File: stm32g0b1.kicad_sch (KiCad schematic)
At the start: 2 parts, among them J1 Conn_ST_STDC14, U5 STM32L432KBUx

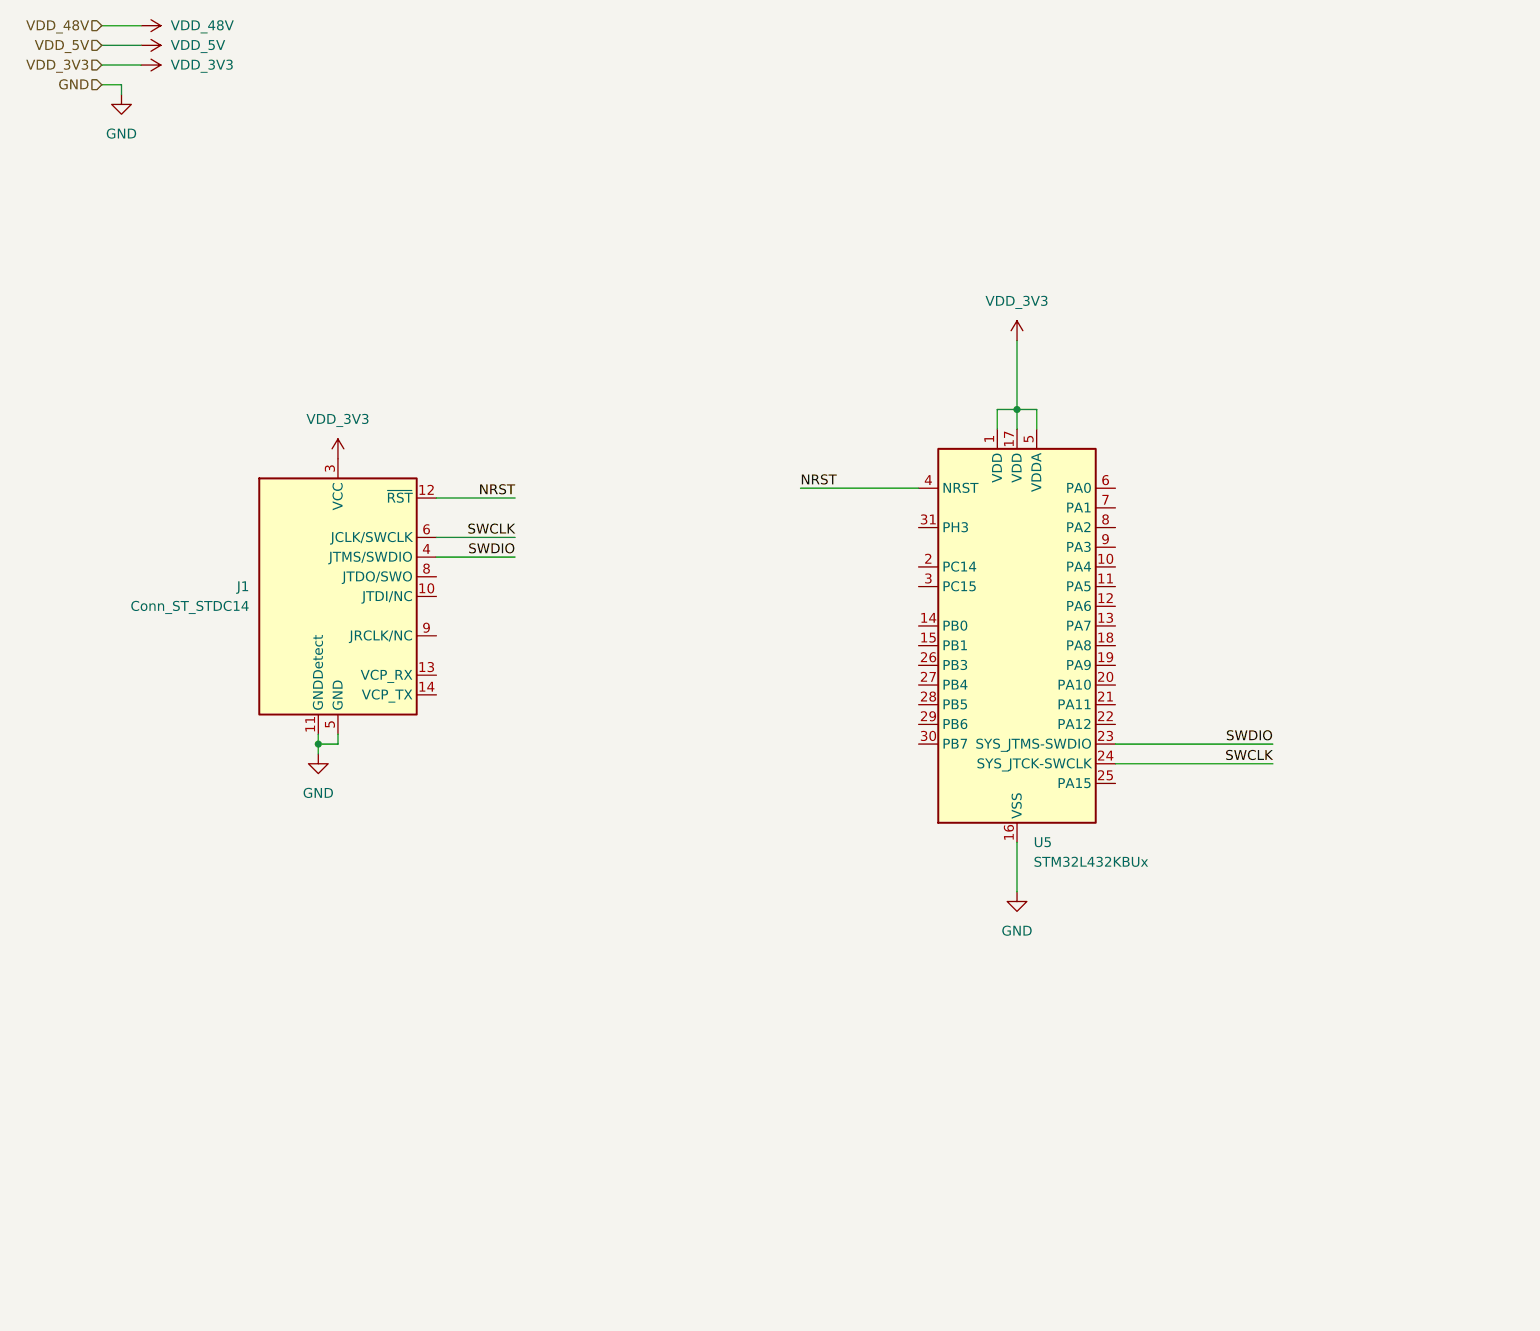
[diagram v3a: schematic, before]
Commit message: fix: fleshignout schematic for mcu, fpga and mag + peripherals
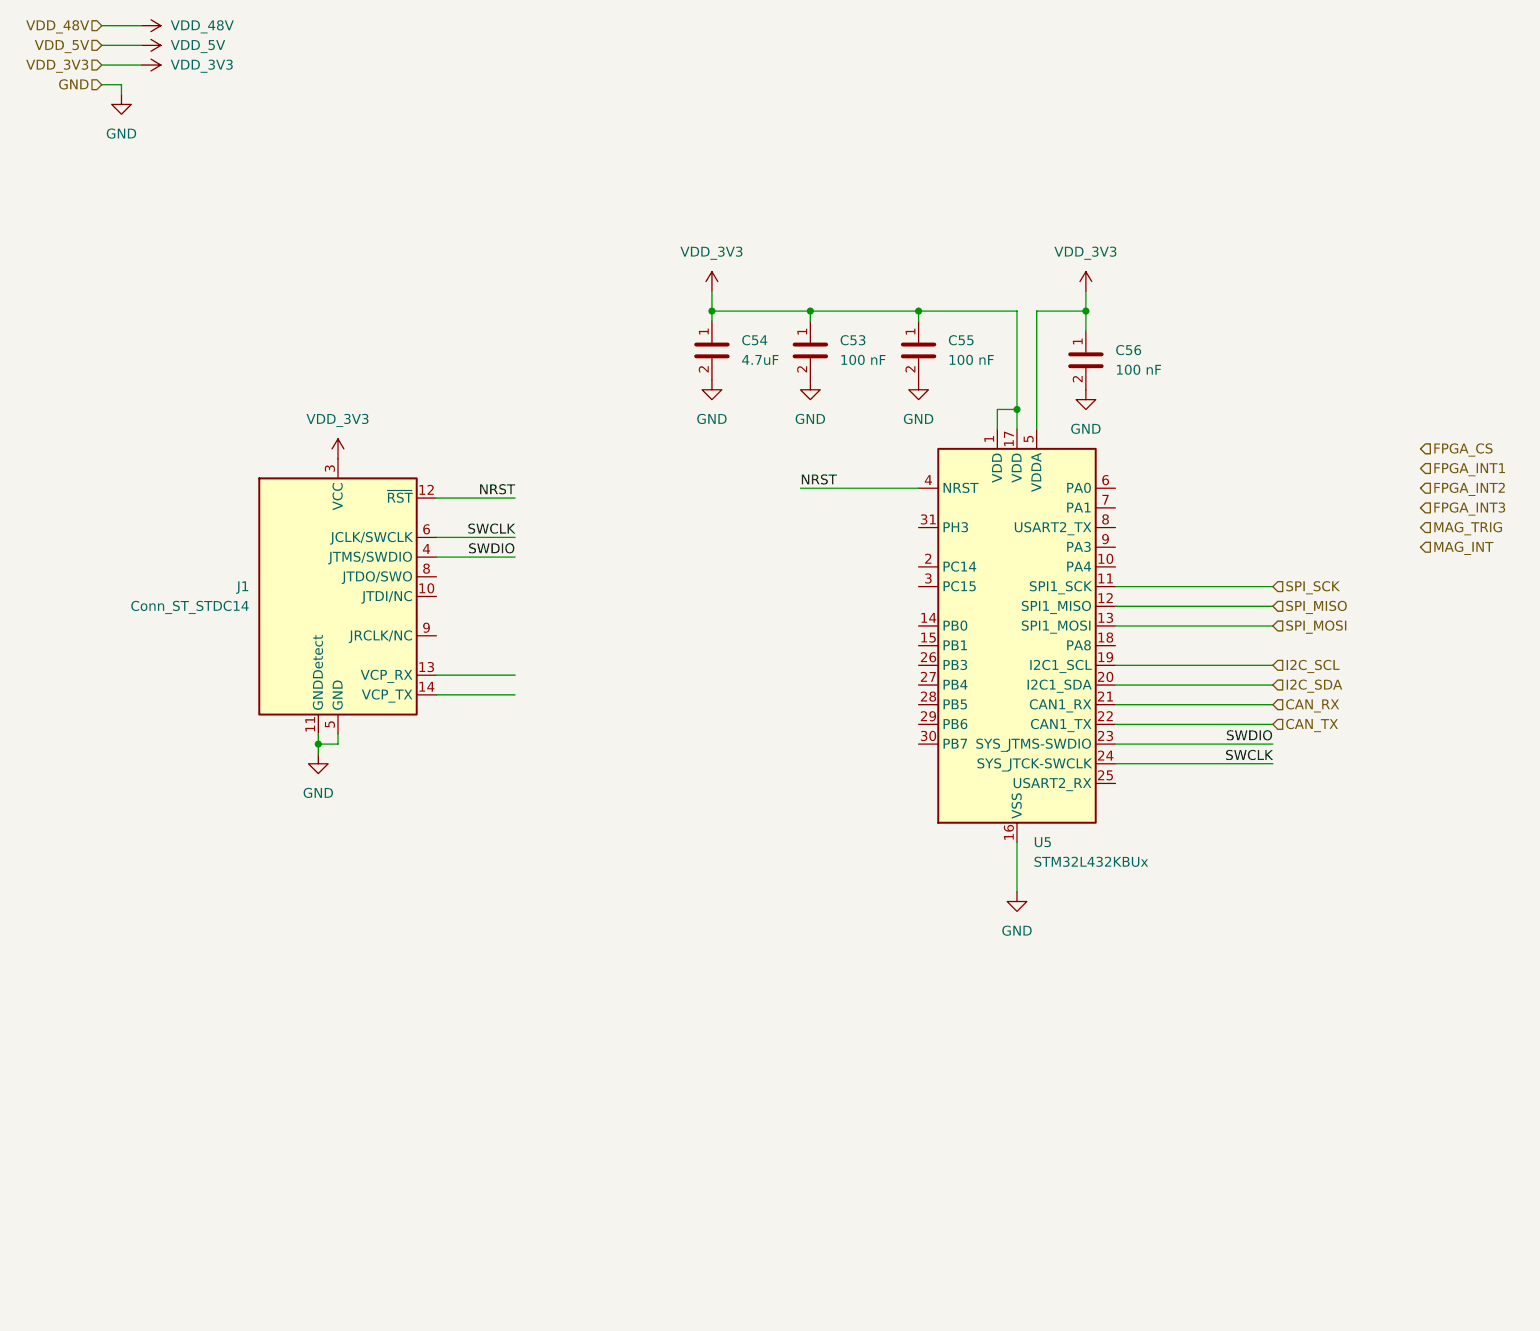
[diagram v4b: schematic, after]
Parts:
- added C53, C55, C56: 100 nF, chenry-footprint-lib:C_0402, symbol 0-chenry-component-lib:C_0402_100N
- added C54: 4.7uF, chenry-footprint-lib:C_0402, symbol 0-chenry-component-lib:C_0402_4U7
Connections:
- net GND: now also C53.2, C54.2, C55.2, C56.2
- net VDD_3V3: now also C53.1, C54.1, C55.1, C56.1
- net SPI_SCK: now reaches U5.11 (PA5)
- net SPI_MISO: now reaches U5.12 (PA6)
- net SPI_MOSI: now reaches U5.13 (PA7)
- net I2C_SCL: now reaches U5.19 (PA9)
- net I2C_SDA: now reaches U5.20 (PA10)
- net CAN_RX: now reaches U5.21 (PA11)
- net CAN_TX: now reaches U5.22 (PA12)

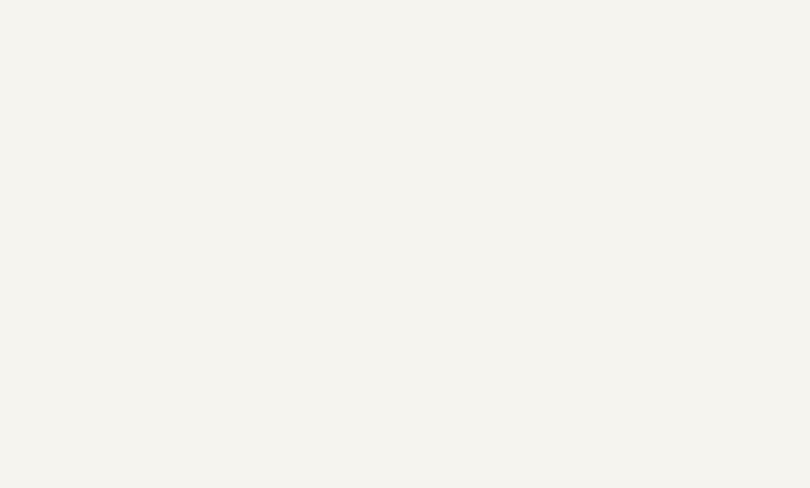
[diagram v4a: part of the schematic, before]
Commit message: fix: adjusting positioning of programmign header
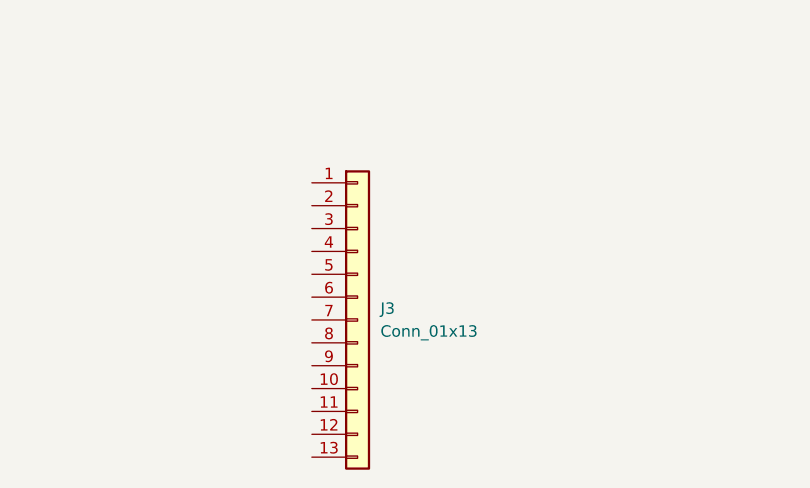
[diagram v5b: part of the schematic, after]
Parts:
- added J3: Conn_01x13, Connector_FFC-FPC:Hirose_FH12-13S-0.5SH_1x13-1MP_P0.50mm_Horizontal, symbol Connector_Generic:Conn_01x13
- J1: footprint Connector_PinHeader_1.27mm:PinHeader_2x07_P1.27mm_Vertical_SMD -> Connector_FFC-FPC:Molex_502231-1500_1x15-1SH_P0.5mm_Vertical
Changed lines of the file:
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@@
 			)
 		)
-		(property "Footprint" "Connector_PinHeader_1.27mm:PinHeader_2x07_P1.27mm_Vertical_SMD"
+		(property "Footprint" "Connector_FFC-FPC:Molex_502231-1500_1x15-1SH_P0.5mm_Vertical"
 			(at 54.61 90.17 0)
 			(effects
@@
 					(unit 1)
 				)
+			)
+		)
+	)
+	(symbol
+		(lib_id "Connector_Generic:Conn_01x13")
+		(at 57.15 166.37 0)
+		(unit 1)
+		(exclude_from_sim no)
+		(in_bom yes)
+		(on_board yes)
+		(dnp no)
+		(fields_autoplaced yes)
+		(property "Reference" "J3"
+			(at 59.69 165.0999 0)
+			(effects
+				(font
+					(size 1.27 1.27)
+				)
+				(justify left)
+			)
+		)
+		(property "Value" "Conn_01x13"
+			(at 59.69 167.6399 0)
+			(effects
+				(font
+					(size 1.27 1.27)
+				)
+				(justify left)
+			)
+		)
+		(property "Footprint" "Connector_FFC-FPC:Hirose_FH12-13S-0.5SH_1x13-1MP_P0.50mm_Horizontal"
+			(at 57.15 166.37 0)
+			(effects
+				(font
+					(size 1.27 1.27)
+				)
+				(hide yes)
+			)
+		)
+		(property "Datasheet" "~"
+			(at 57.15 166.37 0)
+			(effects
+				(font
+					(size 1.27 1.27)
+				)
+				(hide yes)
+			)
+		)
+		(property "Description" "Generic connector, single row, 01x13, script generated (kicad-library-utils/schlib/autogen/connector/)"
+			(at 57.15 166.37 0)
+			(effects
+				(font
+					(size 1.27 1.27)
+				)
+				(hide yes)
+			)
+		)
+		(property "MFR_PN1" ""
+			(at 57.15 166.37 0)
+			(effects
+				(font
+					(size 1.27 1.27)
+				)
+				(hide yes)
+			)
+		)
+		(property "MFR_PN2" ""
+			(at 57.15 166.37 0)
+			(effects
+				(font
+					(size 1.27 1.27)
+				)
+				(hide yes)
+			)
+		)
+		(property "MFR_PN3" ""
+			(at 57.15 166.37 0)
+			(effects
+				(font
+					(size 1.27 1.27)
+				)
+				(hide yes)
+			)
+		)
+		(property "JLC_PN" ""
+			(at 57.15 166.37 0)
+			(effects
+				(font
+					(size 1.27 1.27)
+				)
+				(hide yes)
+			)
+		)
+		(pin "7"
+		)
+		(pin "5"
+		)
+		(pin "10"
+		)
+		(pin "6"
+		)
+		(pin "11"
+		)
+		(pin "8"
+		)
+		(pin "9"
+		)
+		(pin "12"
+		)
+		(pin "13"
+		)
+		(pin "3"
+		)
+		(pin "1"
+		)
+		(pin "2"
+		)
+		(pin "4"
+		)
+		(instances
+			(project ""
+				(path "/e1f256b3-686f-4e34-9512-fa5de8536fd7/0cb427d4-6402-4c72-8ad8-57931fc8c658"
+					(reference "J3")
+					(unit 1)
+				)
